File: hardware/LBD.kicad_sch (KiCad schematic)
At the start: 19 parts, among them J1 Conn_01x03_Pin, U1 RP2040, Y1 12 MHz

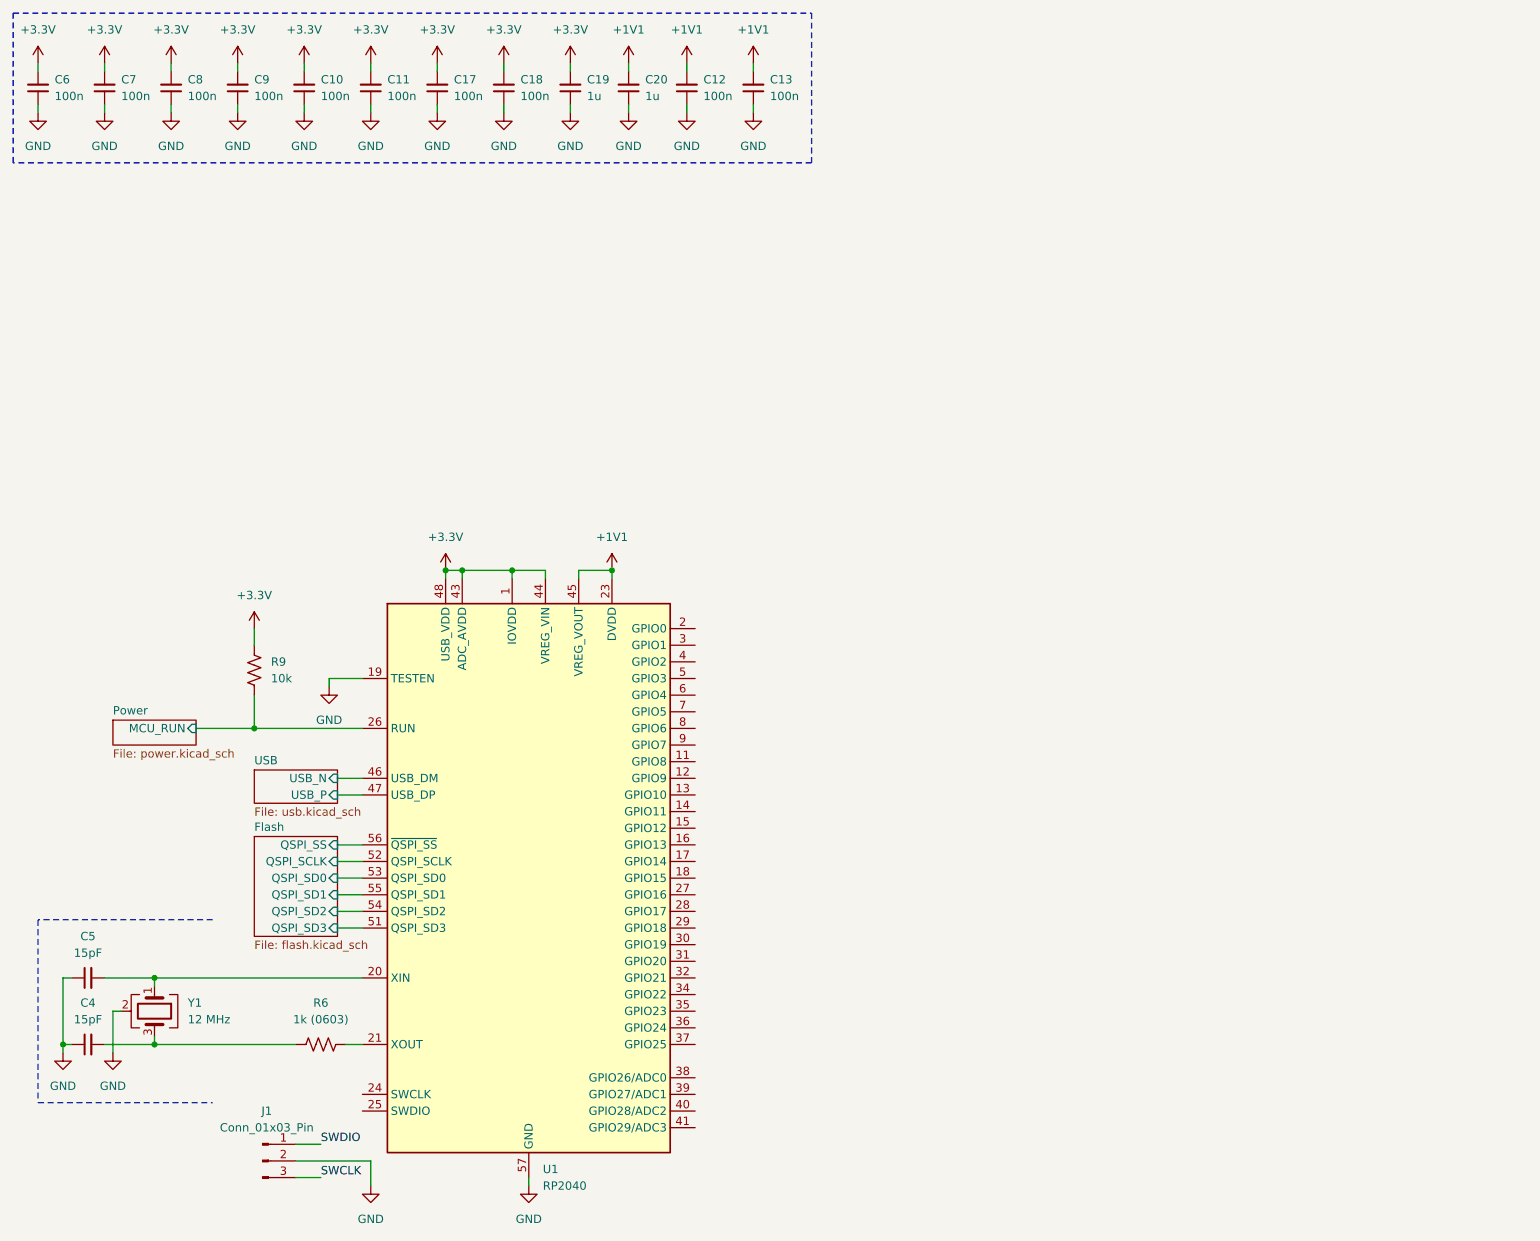
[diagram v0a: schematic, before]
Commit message: started placing leds
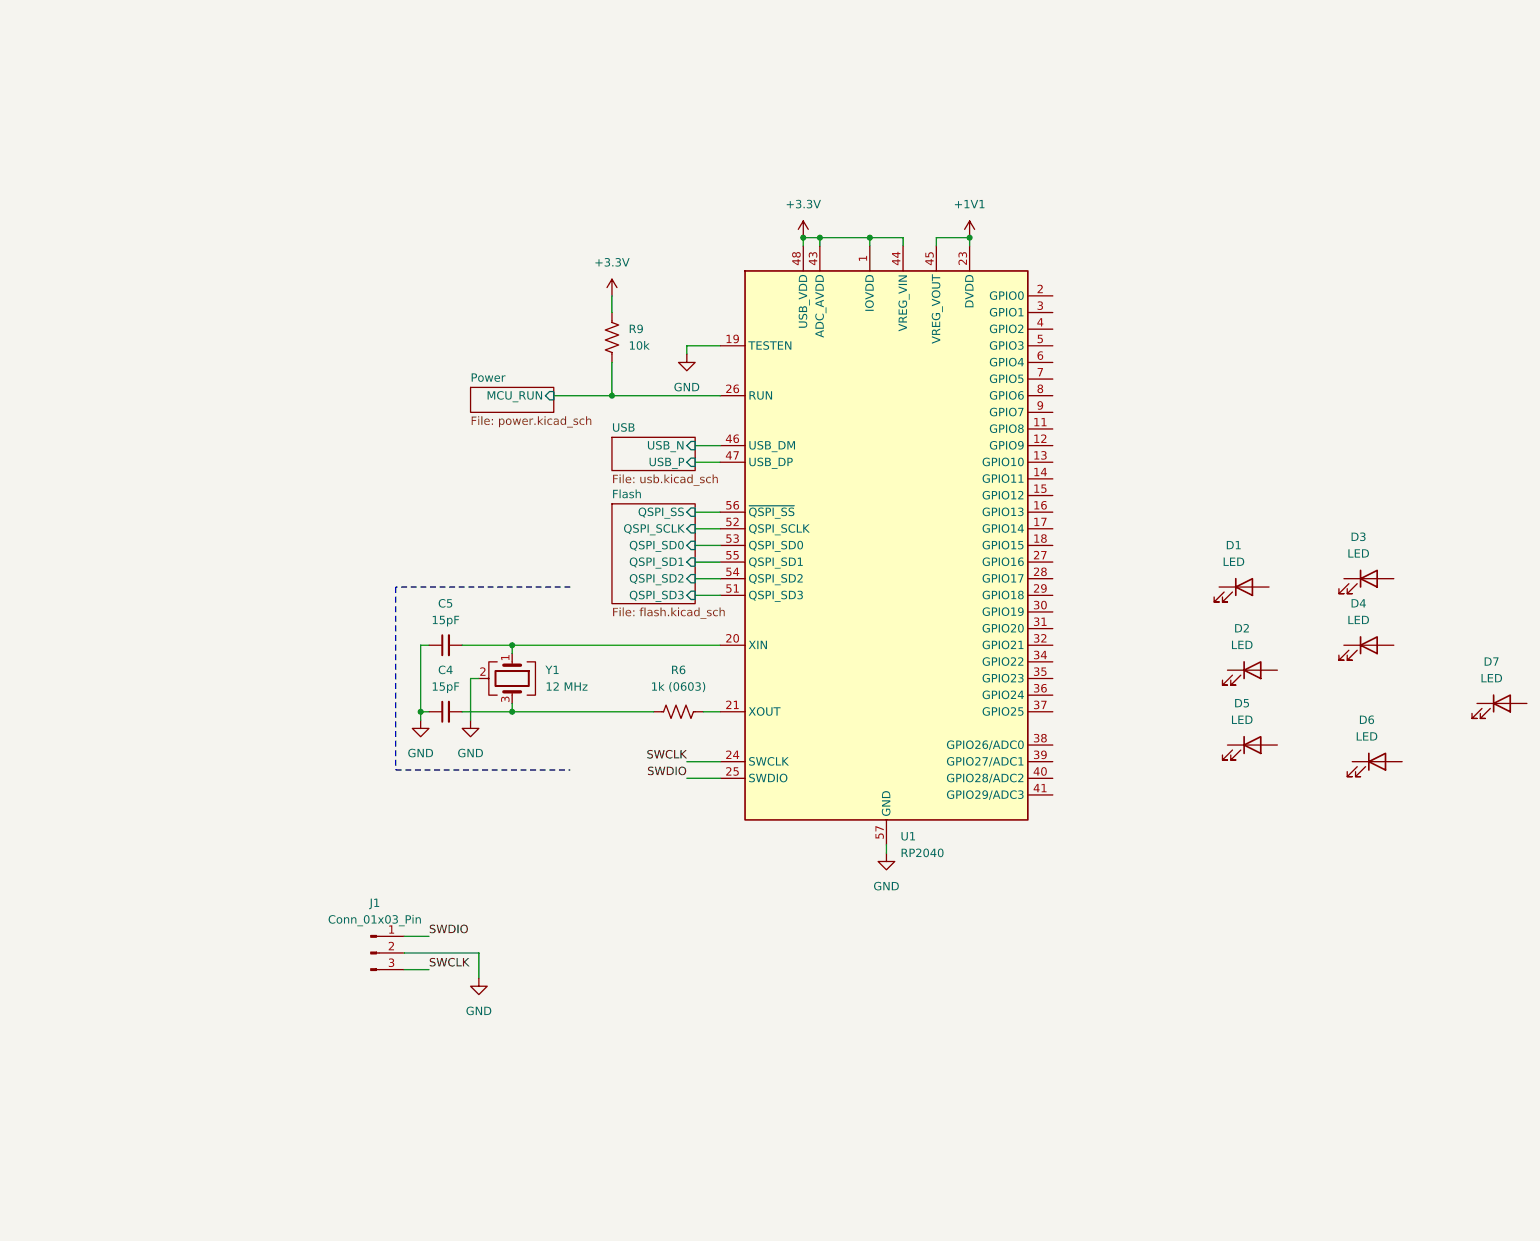
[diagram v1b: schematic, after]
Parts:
- removed C10, C11, C12, C13, C17, C18, C6, C7, C8, C9: 100n, symbol Device:C_Small
- removed C19, C20: 1u, symbol Device:C_Small
- added D1, D2, D3, D4, D5, D6, D7: LED, LBD_Footprints:LED_IN-S12_INL, symbol Device:LED
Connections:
- net SWCLK: now also U1.24 (SWCLK)
- net SWDIO: now also U1.25 (SWDIO)
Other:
- moved on the sheet: C4, C5, J1, R6, R9, U1, Y1
